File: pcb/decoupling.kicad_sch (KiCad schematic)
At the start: 0 parts

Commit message: decoupling
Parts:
- added C? (x22): 0.1uF, Capacitor_SMD:C_0402_1005Metric, symbol Device:C
- added C?: 47uF, Capacitor_SMD:C_0402_1005Metric, symbol Device:C
- added C?: 10uF, Capacitor_SMD:C_0402_1005Metric, symbol Device:C
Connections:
- net +1V0_FD: now also C?.1, C?.1, C?.1, C?.1, C?.1, C?.1, C?.1, C?.1, C?.1, C?.1, C?.1, C?.1, C?.1, C?.1, C?.1, C?.1, C?.1, C?.1, C?.1, C?.1, C?.1, C?.1, C?.1, C?.1

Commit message: decoupling
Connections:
- net GND: now reaches C?.2
- net GND: now also C?.2, C?.2, C?.2, C?.2, C?.2, C?.2, C?.2, C?.2, C?.2, C?.2, C?.2, C?.2, C?.2, C?.2, C?.2, C?.2, C?.2, C?.2, C?.2, C?.2, C?.2, C?.2, C?.2

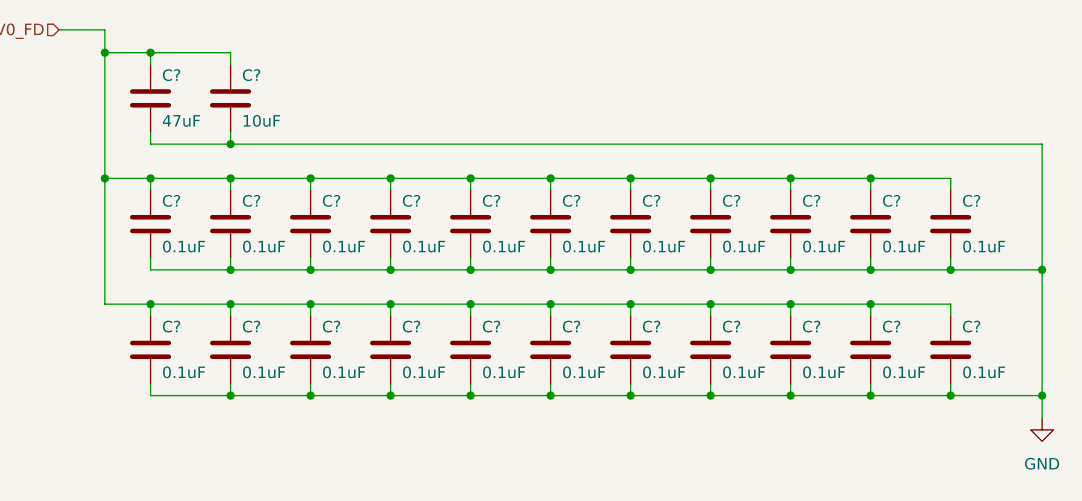
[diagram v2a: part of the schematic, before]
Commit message: changed spi flash to wson
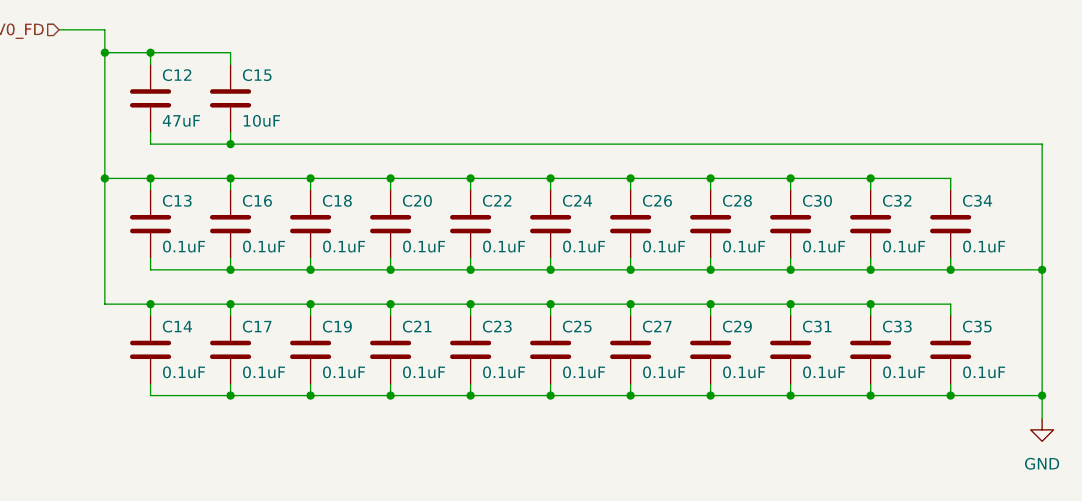
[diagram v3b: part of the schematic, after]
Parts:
- C12: renamed from C?; footprint Capacitor_SMD:C_0402_1005Metric -> Capacitor_SMD:C_0603_1608Metric
- C14, C16, C17, C18, C19, C20, C21, C22, C23, C24, C25, C26, C27, C28, C29, C30, C31, C32, C33, C34, C35: renamed from C?; footprint Capacitor_SMD:C_0402_1005Metric -> Capacitor_SMD:C_0201_0603Metric
- gave numbers to parts that had none: 2

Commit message: fpga decoupling
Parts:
- added C? (x14): 0.1uF, Capacitor_SMD:C_0201_0603Metric, symbol Device:C
- added C? (x2): 10uF, Capacitor_SMD:C_0402_1005Metric, symbol Device:C
- added C? (x2): 47uF, Capacitor_SMD:C_0603_1608Metric, symbol Device:C
- added C? (x3): 0.1uF, Capacitor_SMD:C_0402_1005Metric, symbol Device:C
- added C?: 10uF, Capacitor_SMD:C_0603_1608Metric, symbol Device:C
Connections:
- net GND: now also C?.2, C?.2, C?.2, C?.2, C?.2, C?.2, C?.2, C?.2, C?.2, C?.2, C?.2, C?.2, C?.2, C?.2, C?.2, C?.2, C?.2, C?.2, C?.2, C?.2, C?.2, C?.2
- net +1V0_FD renamed 1V0_FD
- new net 1V0_MGT: C?.1, C?.1, C?.1, C?.1, C?.1, C?.1
- new net 1V2_MGT: C?.1, C?.1, C?.1, C?.1, C?.1, C?.1, C?.1, C?.1
- new net 1V8_FD: C?.1, C?.1, C?.1, C?.1, C?.1, C?.1, C?.1, C?.1
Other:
- moved on the sheet: C12, C13, C14, C15, C16, C17, C18, C19, C20, C21, C22, C23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

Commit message: pcie definitions
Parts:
- gave numbers to parts that had none: 22
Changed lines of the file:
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@@
 		(on_board yes)
 		(dnp no)
-		(property "Reference" "C?"
+		(property "Reference" "C61"
 			(at 109.22 134.62 0)
 			(effects
@@
 			(project "RPi-HwAB-1"
 				(path "/e63e39d7-6ac0-4ffd-8aa3-1841a4541b55/59d21473-a004-4514-8090-fd93db818925/94db1840-7840-4b32-9939-76c2575d480c/d1fe51bb-390e-4bc5-afb0-b85902b013c3"
-					(reference "C?")
+					(reference "C61")
 					(unit 1)
 				)
@@
 		(on_board yes)
 		(dnp no)
-		(property "Reference" "C?"
+		(property "Reference" "C58"
 			(at 100.33 134.62 0)
 			(effects
@@
 			(project "RPi-HwAB-1"
 				(path "/e63e39d7-6ac0-4ffd-8aa3-1841a4541b55/59d21473-a004-4514-8090-fd93db818925/94db1840-7840-4b32-9939-76c2575d480c/d1fe51bb-390e-4bc5-afb0-b85902b013c3"
-					(reference "C?")
+					(reference "C58")
 					(unit 1)
 				)
@@
 		(on_board yes)
 		(dnp no)
-		(property "Reference" "C?"
+		(property "Reference" "C48"
 			(at 67.31 134.62 0)
 			(effects
@@
 			(project "RPi-HwAB-1"
 				(path "/e63e39d7-6ac0-4ffd-8aa3-1841a4541b55/59d21473-a004-4514-8090-fd93db818925/94db1840-7840-4b32-9939-76c2575d480c/d1fe51bb-390e-4bc5-afb0-b85902b013c3"
-					(reference "C?")
+					(reference "C48")
 					(unit 1)
 				)
@@
 		(on_board yes)
 		(dnp no)
-		(property "Reference" "C?"
+		(property "Reference" "C50"
 			(at 80.01 86.36 0)
 			(effects
@@
 			(project "RPi-HwAB-1"
 				(path "/e63e39d7-6ac0-4ffd-8aa3-1841a4541b55/59d21473-a004-4514-8090-fd93db818925/94db1840-7840-4b32-9939-76c2575d480c/d1fe51bb-390e-4bc5-afb0-b85902b013c3"
-					(reference "C?")
+					(reference "C50")
 					(unit 1)
 				)
@@
 		(on_board yes)
 		(dnp no)
-		(property "Reference" "C?"
+		(property "Reference" "C59"
 			(at 106.68 86.36 0)
 			(effects
@@
 			(project "RPi-HwAB-1"
 				(path "/e63e39d7-6ac0-4ffd-8aa3-1841a4541b55/59d21473-a004-4514-8090-fd93db818925/94db1840-7840-4b32-9939-76c2575d480c/d1fe51bb-390e-4bc5-afb0-b85902b013c3"
-					(reference "C?")
+					(reference "C59")
 					(unit 1)
 				)
@@
 		(on_board yes)
 		(dnp no)
-		(property "Reference" "C?"
+		(property "Reference" "C45"
 			(at 58.42 110.49 0)
 			(effects
@@
 			(project "RPi-HwAB-1"
 				(path "/e63e39d7-6ac0-4ffd-8aa3-1841a4541b55/59d21473-a004-4514-8090-fd93db818925/94db1840-7840-4b32-9939-76c2575d480c/d1fe51bb-390e-4bc5-afb0-b85902b013c3"
-					(reference "C?")
+					(reference "C45")
 					(unit 1)
 				)
@@
 		(on_board yes)
 		(dnp no)
-		(property "Reference" "C?"
+		(property "Reference" "C47"
 			(at 67.31 110.49 0)
 			(effects
@@
 			(project "RPi-HwAB-1"
 				(path "/e63e39d7-6ac0-4ffd-8aa3-1841a4541b55/59d21473-a004-4514-8090-fd93db818925/94db1840-7840-4b32-9939-76c2575d480c/d1fe51bb-390e-4bc5-afb0-b85902b013c3"
-					(reference "C?")
+					(reference "C47")
 					(unit 1)
 				)
@@
 		(on_board yes)
 		(dnp no)
-		(property "Reference" "C?"
+		(property "Reference" "C52"
 			(at 82.55 134.62 0)
 			(effects
@@
 			(project "RPi-HwAB-1"
 				(path "/e63e39d7-6ac0-4ffd-8aa3-1841a4541b55/59d21473-a004-4514-8090-fd93db818925/94db1840-7840-4b32-9939-76c2575d480c/d1fe51bb-390e-4bc5-afb0-b85902b013c3"
-					(reference "C?")
+					(reference "C52")
 					(unit 1)
 				)
@@
 		(on_board yes)
 		(dnp no)
-		(property "Reference" "C?"
+		(property "Reference" "C49"
 			(at 71.12 86.36 0)
 			(effects
@@
 			(project "RPi-HwAB-1"
 				(path "/e63e39d7-6ac0-4ffd-8aa3-1841a4541b55/59d21473-a004-4514-8090-fd93db818925/94db1840-7840-4b32-9939-76c2575d480c/d1fe51bb-390e-4bc5-afb0-b85902b013c3"
-					(reference "C?")
+					(reference "C49")
 					(unit 1)
 				)
@@
 		(on_board yes)
 		(dnp no)
-		(property "Reference" "C?"
+		(property "Reference" "C63"
 			(at 118.11 134.62 0)
 			(effects
@@
 			(project "RPi-HwAB-1"
 				(path "/e63e39d7-6ac0-4ffd-8aa3-1841a4541b55/59d21473-a004-4514-8090-fd93db818925/94db1840-7840-4b32-9939-76c2575d480c/d1fe51bb-390e-4bc5-afb0-b85902b013c3"
-					(reference "C?")
+					(reference "C63")
 					(unit 1)
 				)
@@
 		(on_board yes)
 		(dnp no)
-		(property "Reference" "C?"
+		(property "Reference" "C54"
 			(at 91.44 110.49 0)
 			(effects
@@
 			(project "RPi-HwAB-1"
 				(path "/e63e39d7-6ac0-4ffd-8aa3-1841a4541b55/59d21473-a004-4514-8090-fd93db818925/94db1840-7840-4b32-9939-76c2575d480c/d1fe51bb-390e-4bc5-afb0-b85902b013c3"
-					(reference "C?")
+					(reference "C54")
 					(unit 1)
 				)
@@
 		(on_board yes)
 		(dnp no)
-		(property "Reference" "C?"
+		(property "Reference" "C55"
 			(at 91.44 134.62 0)
 			(effects
@@
 			(project "RPi-HwAB-1"
 				(path "/e63e39d7-6ac0-4ffd-8aa3-1841a4541b55/59d21473-a004-4514-8090-fd93db818925/94db1840-7840-4b32-9939-76c2575d480c/d1fe51bb-390e-4bc5-afb0-b85902b013c3"
-					(reference "C?")
+					(reference "C55")
 					(unit 1)
 				)
@@
 		(on_board yes)
 		(dnp no)
-		(property "Reference" "C?"
+		(property "Reference" "C51"
 			(at 82.55 110.49 0)
 			(effects
@@
 			(project "RPi-HwAB-1"
 				(path "/e63e39d7-6ac0-4ffd-8aa3-1841a4541b55/59d21473-a004-4514-8090-fd93db818925/94db1840-7840-4b32-9939-76c2575d480c/d1fe51bb-390e-4bc5-afb0-b85902b013c3"
-					(reference "C?")
+					(reference "C51")
 					(unit 1)
 				)
@@
 		(on_board yes)
 		(dnp no)
-		(property "Reference" "C?"
+		(property "Reference" "C53"
 			(at 88.9 86.36 0)
 			(effects
@@
 			(project "RPi-HwAB-1"
 				(path "/e63e39d7-6ac0-4ffd-8aa3-1841a4541b55/59d21473-a004-4514-8090-fd93db818925/94db1840-7840-4b32-9939-76c2575d480c/d1fe51bb-390e-4bc5-afb0-b85902b013c3"
-					(reference "C?")
+					(reference "C53")
 					(unit 1)
 				)
@@
 		(on_board yes)
 		(dnp no)
-		(property "Reference" "C?"
+		(property "Reference" "C57"
 			(at 100.33 110.49 0)
 			(effects
@@
 			(project "RPi-HwAB-1"
 				(path "/e63e39d7-6ac0-4ffd-8aa3-1841a4541b55/59d21473-a004-4514-8090-fd93db818925/94db1840-7840-4b32-9939-76c2575d480c/d1fe51bb-390e-4bc5-afb0-b85902b013c3"
-					(reference "C?")
+					(reference "C57")
 					(unit 1)
 				)
@@
 		(on_board yes)
 		(dnp no)
-		(property "Reference" "C?"
+		(property "Reference" "C60"
 			(at 109.22 110.49 0)
 			(effects
@@
 			(project "RPi-HwAB-1"
 				(path "/e63e39d7-6ac0-4ffd-8aa3-1841a4541b55/59d21473-a004-4514-8090-fd93db818925/94db1840-7840-4b32-9939-76c2575d480c/d1fe51bb-390e-4bc5-afb0-b85902b013c3"
-					(reference "C?")
+					(reference "C60")
 					(unit 1)
 				)
@@
 		(on_board yes)
 		(dnp no)
-		(property "Reference" "C?"
+		(property "Reference" "C64"
 			(at 127 110.49 0)
 			(effects
@@
 			(project "RPi-HwAB-1"
 				(path "/e63e39d7-6ac0-4ffd-8aa3-1841a4541b55/59d21473-a004-4514-8090-fd93db818925/94db1840-7840-4b32-9939-76c2575d480c/d1fe51bb-390e-4bc5-afb0-b85902b013c3"
-					(reference "C?")
+					(reference "C64")
 					(unit 1)
 				)
@@
 		(on_board yes)
 		(dnp no)
-		(property "Reference" "C?"
+		(property "Reference" "C62"
 			(at 118.11 110.49 0)
 			(effects
@@
 			(project "RPi-HwAB-1"
 				(path "/e63e39d7-6ac0-4ffd-8aa3-1841a4541b55/59d21473-a004-4514-8090-fd93db818925/94db1840-7840-4b32-9939-76c2575d480c/d1fe51bb-390e-4bc5-afb0-b85902b013c3"
-					(reference "C?")
+					(reference "C62")
 					(unit 1)
 				)
@@
 		(on_board yes)
 		(dnp no)
-		(property "Reference" "C?"
+		(property "Reference" "C46"
 			(at 58.42 134.62 0)
 			(effects
@@
 			(project "RPi-HwAB-1"
 				(path "/e63e39d7-6ac0-4ffd-8aa3-1841a4541b55/59d21473-a004-4514-8090-fd93db818925/94db1840-7840-4b32-9939-76c2575d480c/d1fe51bb-390e-4bc5-afb0-b85902b013c3"
-					(reference "C?")
+					(reference "C46")
 					(unit 1)
 				)
@@
 		(on_board yes)
 		(dnp no)
-		(property "Reference" "C?"
+		(property "Reference" "C56"
 			(at 97.79 86.36 0)
 			(effects
@@
 			(project "RPi-HwAB-1"
 				(path "/e63e39d7-6ac0-4ffd-8aa3-1841a4541b55/59d21473-a004-4514-8090-fd93db818925/94db1840-7840-4b32-9939-76c2575d480c/d1fe51bb-390e-4bc5-afb0-b85902b013c3"
-					(reference "C?")
+					(reference "C56")
 					(unit 1)
 				)
@@
 		(on_board yes)
 		(dnp no)
-		(property "Reference" "C?"
+		(property "Reference" "C65"
 			(at 127 134.62 0)
 			(effects
@@
 			(project "RPi-HwAB-1"
 				(path "/e63e39d7-6ac0-4ffd-8aa3-1841a4541b55/59d21473-a004-4514-8090-fd93db818925/94db1840-7840-4b32-9939-76c2575d480c/d1fe51bb-390e-4bc5-afb0-b85902b013c3"
-					(reference "C?")
+					(reference "C65")
 					(unit 1)
 				)
@@
 		(on_board yes)
 		(dnp no)
-		(property "Reference" "C?"
+		(property "Reference" "C44"
 			(at 57.15 86.36 0)
 			(effects
@@
 			(project "RPi-HwAB-1"
 				(path "/e63e39d7-6ac0-4ffd-8aa3-1841a4541b55/59d21473-a004-4514-8090-fd93db818925/94db1840-7840-4b32-9939-76c2575d480c/d1fe51bb-390e-4bc5-afb0-b85902b013c3"
-					(reference "C?")
+					(reference "C44")
 					(unit 1)
 				)

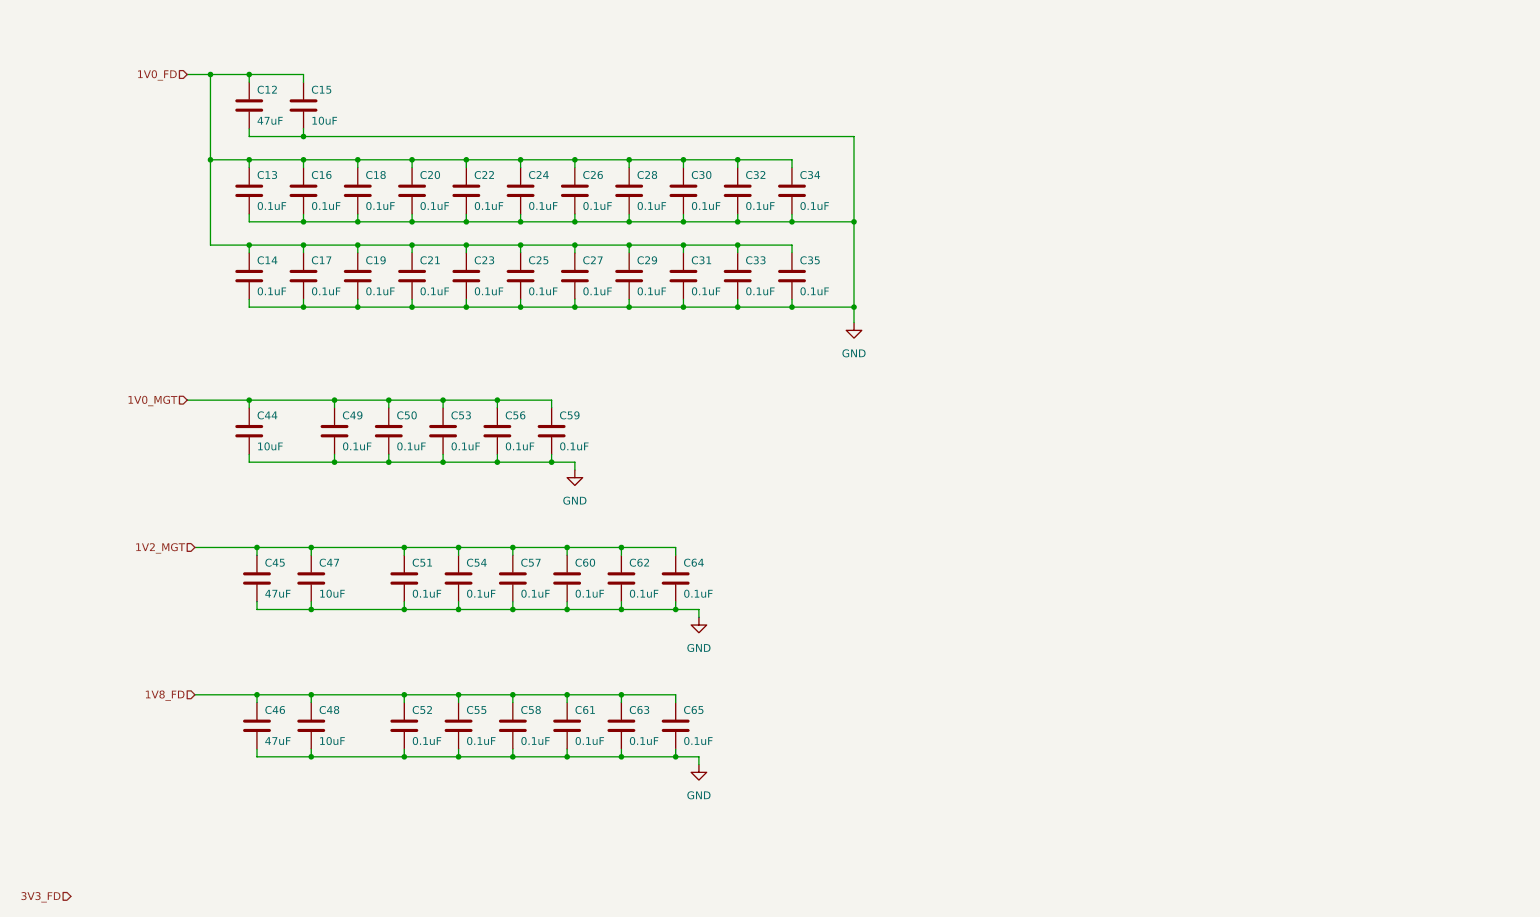
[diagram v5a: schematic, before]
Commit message: decoupling for 3v3_fd
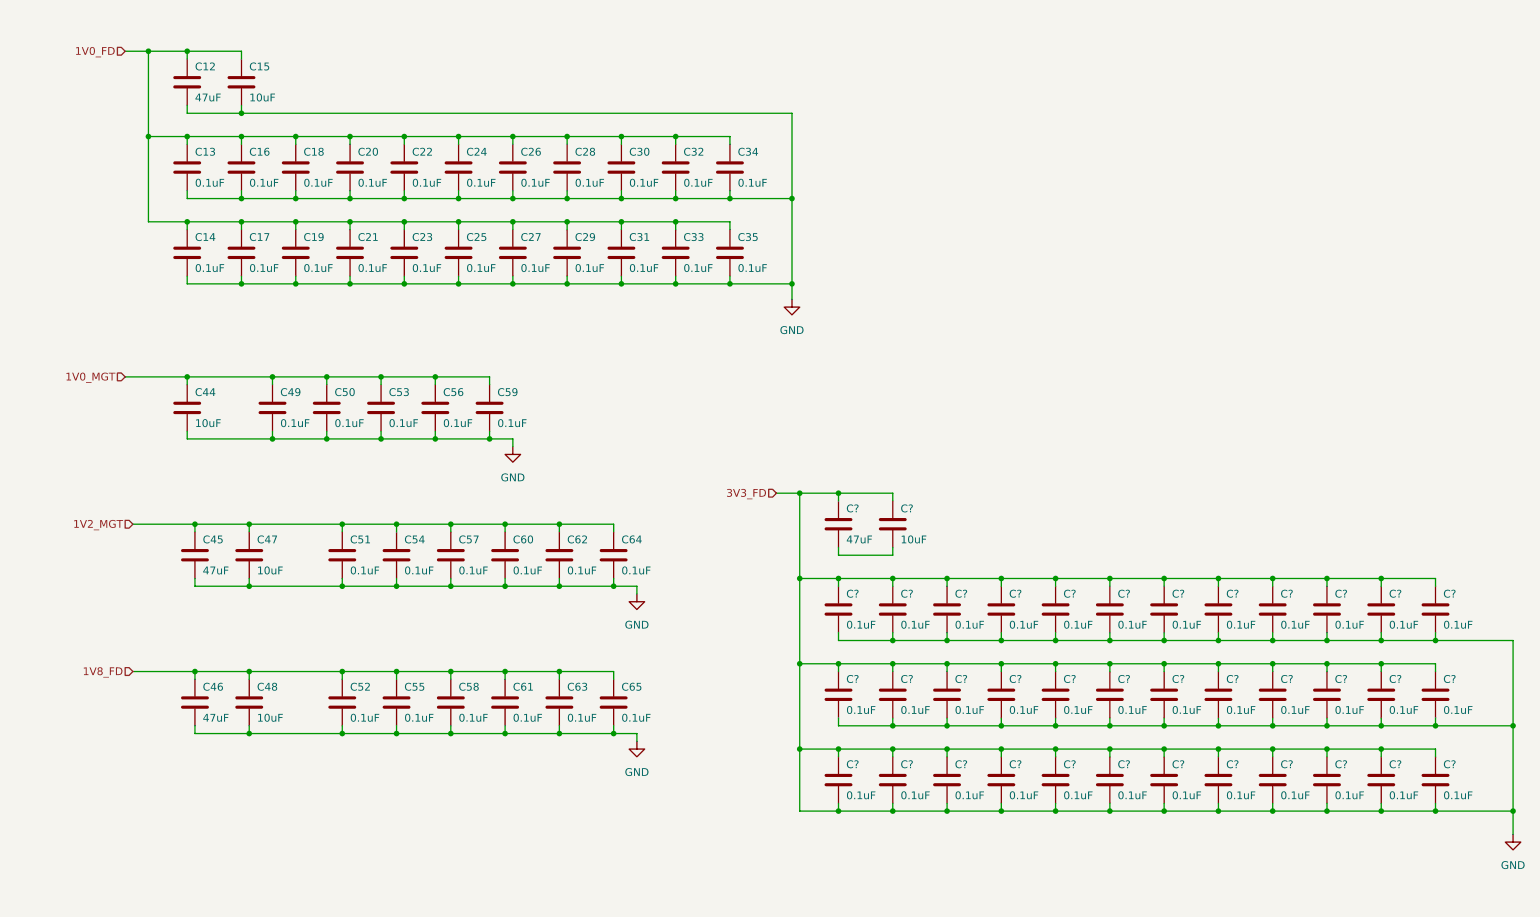
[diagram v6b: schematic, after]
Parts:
- added C? (x35): 0.1uF, Capacitor_SMD:C_0201_0603Metric, symbol Device:C
- added C?: 0.1uF, Capacitor_SMD:C_0402_1005Metric, symbol Device:C
- added C?: 47uF, Capacitor_SMD:C_0603_1608Metric, symbol Device:C
- added C?: 10uF, Capacitor_SMD:C_0402_1005Metric, symbol Device:C
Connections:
- net GND: now also C?.1, C?.1, C?.1, C?.1, C?.1, C?.1, C?.1, C?.1, C?.1, C?.1, C?.1, C?.1, C?.1, C?.1, C?.1, C?.1, C?.1, C?.1, C?.1, C?.1, C?.1, C?.1, C?.1, C?.1, C?.1, C?.1, C?.1, C?.1, C?.1, C?.1, C?.1, C?.1, C?.1, C?.1, C?.1, C?.1, C?.1, C?.1, C?.2, C?.2, C?.2, C?.2, C?.2, C?.2, C?.2, C?.2, C?.2, C?.2, C?.2, C?.2, C?.2, C?.2, C?.2, C?.2, C?.2, C?.2, C?.2, C?.2, C?.2, C?.2, C?.2, C?.2, C?.2, C?.2, C?.2, C?.2, C?.2, C?.2, C?.2, C?.2, C?.2, C?.2, C?.2, C?.2
- new net: C?.2, C?.2
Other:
- moved on the sheet: C12, C13, C14, C15, C16, C17, C18, C19, C20, C21, C22, C23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

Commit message: ddr3
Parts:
- gave numbers to parts that had none: 38

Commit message: saved libraries to project
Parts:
- C100, C101, C12, C13, C14, C15, C16, C17, C18, C19, C20, C21, C22, C23, C24, C25, C26, C27, C28, C29, C3, C30, C31, C32, C33, C34, C35, C44, C45, C46, C47, C48, C49, C5, C50, C51, C52, C53, C54, C55, C56, C57, C58, C59, C60, C61, C62, C63, C64, C65, C66, C67, C68, C69, C70, C71, C72, C73, C74, C75, C76, C77, C78, C79, C80, C81, C82, C83, C84, C85, C86, C87, C88, C89, C90, C91, C92, C93, C94, C95, C96, C97, C98, C99: symbol Device:C -> library:C
